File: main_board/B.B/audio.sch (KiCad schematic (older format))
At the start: 34 parts

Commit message: konzultace_s_Kubou_01
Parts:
- added C?: 1uf, Resistor_SMD:R_0402_1005Metric, symbol Device:C
- added C? (x2): 0.1uf, Resistor_SMD:R_0402_1005Metric, symbol Device:C
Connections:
- net 5V: now also C?.1, C?.1
- net at U?.4 (PB): now also C?.1
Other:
- moved on the sheet: C?, J?, LS?, MK?, R?, e

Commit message: preparation_to_drawing_PCB
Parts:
- J?: footprint (none) -> BB:JC-128
- LS? (x2), MK? (x2): footprint (none) -> Connector_PinHeader_2.54mm:PinHeader_1x02_P2.54mm_Vertical
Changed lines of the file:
@@
 F 0 "LS?" H 4070 5346 50  0000 L CNN
 F 1 "Speaker" H 4070 5255 50  0000 L CNN
-F 2 "" H 3900 5150 50  0001 C CNN
+F 2 "Connector_PinHeader_2.54mm:PinHeader_1x02_P2.54mm_Vertical" H 3900 5150 50  0001 C CNN
 F 3 "~" H 3890 5300 50  0001 C CNN
 	1    3900 5350
@@
 F 0 "LS?" H 4070 5046 50  0000 L CNN
 F 1 "Speaker" H 4070 4955 50  0000 L CNN
-F 2 "" H 3900 4850 50  0001 C CNN
+F 2 "Connector_PinHeader_2.54mm:PinHeader_1x02_P2.54mm_Vertical" H 3900 4850 50  0001 C CNN
 F 3 "~" H 3890 5000 50  0001 C CNN
 	1    3900 5050
@@
 F 0 "MK?" H 8670 5004 50  0000 R CNN
 F 1 "Microphone" H 8670 5095 50  0000 R CNN
-F 2 "" V 8800 5150 50  0001 C CNN
+F 2 "Connector_PinHeader_2.54mm:PinHeader_1x02_P2.54mm_Vertical" V 8800 5150 50  0001 C CNN
 F 3 "~" V 8800 5150 50  0001 C CNN
 	1    8800 5050
@@
 F 0 "MK?" H 10070 5004 50  0000 R CNN
 F 1 "Microphone" H 10070 5095 50  0000 R CNN
-F 2 "" V 10200 5150 50  0001 C CNN
+F 2 "Connector_PinHeader_2.54mm:PinHeader_1x02_P2.54mm_Vertical" V 10200 5150 50  0001 C CNN
 F 3 "~" V 10200 5150 50  0001 C CNN
 	1    10200 5050
@@
 F 0 "J?" H 9520 2833 50  0000 R CNN
 F 1 "AudioJack4" H 9520 2924 50  0000 R CNN
-F 2 "" H 9850 2950 50  0001 C CNN
+F 2 "BB:JC-128" H 9850 2950 50  0001 C CNN
 F 3 "~" H 9850 2950 50  0001 C CNN
 	1    9850 2950

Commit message: complete_preparation_to_drawing_PCB
footprint for all component and LCSC code for everything for mounting in JLCPCB
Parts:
- e1: renamed from e; footprint Package_DFN_QFN:QFN-20-1EP_4x4mm_P0.5mm_EP2.7x2.7mm -> Package_DFN_QFN:QFN-20-1EP_4x4mm_P0.5mm_EP2.5x2.5mm
- gave numbers to parts that had none: 36

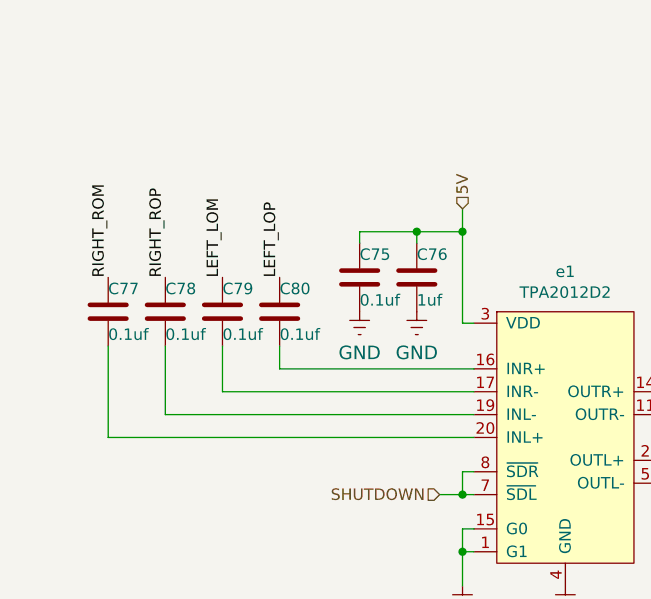
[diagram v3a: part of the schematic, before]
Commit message: optimalizace_kondenzatoru
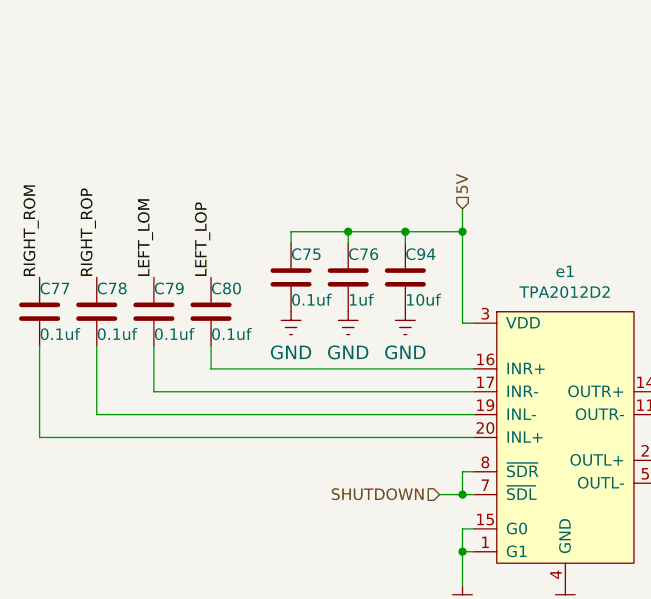
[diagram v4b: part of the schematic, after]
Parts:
- added C94: 10uf, Resistor_SMD:R_0603_1608Metric, symbol Device:C
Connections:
- net 5V: now also C94.1
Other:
- moved on the sheet: C75, C76, C77, C78, C79, C80
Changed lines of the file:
@@
 Text Label 7550 1900 0    50   ~ 0
 LEFT_LOP
-Text Label 1300 4550 1    50   ~ 0
+Text Label 1000 4550 1    50   ~ 0
 RIGHT_ROM
-Text Label 1550 4550 1    50   ~ 0
+Text Label 1250 4550 1    50   ~ 0
 RIGHT_ROP
-Text Label 1800 4550 1    50   ~ 0
+Text Label 1500 4550 1    50   ~ 0
 LEFT_LOM
-Text Label 2050 4550 1    50   ~ 0
+Text Label 1750 4550 1    50   ~ 0
 LEFT_LOP
-Wire Wire Line
-	2850 4250 2850 4350
 Wire Wire Line
 	2850 4750 2900 4750
@@
 L Device:C C80
 U 1 1 5F8B4EB8
-P 2050 4700
-F 0 "C80" H 2050 4800 50  0000 L CNN
-F 1 "0.1uf" H 2050 4600 50  0000 L CNN
-F 2 "Resistor_SMD:R_0402_1005Metric" H 2088 4550 50  0001 C CNN
-F 3 "~" H 2050 4700 50  0001 C CNN
-F 4 "C1525" H 2050 4700 50  0001 C CNN "LCSC"
-	1    2050 4700
-	1    0    0    -1
-$EndComp
-Wire Wire Line
-	2900 4950 2050 4950
-Wire Wire Line
-	2050 4950 2050 4850
+P 1750 4700
+F 0 "C80" H 1750 4800 50  0000 L CNN
+F 1 "0.1uf" H 1750 4600 50  0000 L CNN
+F 2 "Resistor_SMD:R_0402_1005Metric" H 1788 4550 50  0001 C CNN
+F 3 "~" H 1750 4700 50  0001 C CNN
+F 4 "C1525" H 1750 4700 50  0001 C CNN "LCSC"
+	1    1750 4700
+	1    0    0    -1
+$EndComp
+Wire Wire Line
+	2900 4950 1750 4950
+Wire Wire Line
+	1750 4950 1750 4850
 $Comp
 L Device:C C79
 U 1 1 5F8B62DA
-P 1800 4700
-F 0 "C79" H 1800 4800 50  0000 L CNN
-F 1 "0.1uf" H 1800 4600 50  0000 L CNN
-F 2 "Resistor_SMD:R_0402_1005Metric" H 1838 4550 50  0001 C CNN
-F 3 "~" H 1800 4700 50  0001 C CNN
-F 4 "C1525" H 1800 4700 50  0001 C CNN "LCSC"
-	1    1800 4700
+P 1500 4700
+F 0 "C79" H 1500 4800 50  0000 L CNN
+F 1 "0.1uf" H 1500 4600 50  0000 L CNN
+F 2 "Resistor_SMD:R_0402_1005Metric" H 1538 4550 50  0001 C CNN
+F 3 "~" H 1500 4700 50  0001 C CNN
+F 4 "C1525" H 1500 4700 50  0001 C CNN "LCSC"
+	1    1500 4700
 	1    0    0    -1
 $EndComp
@@
 L Device:C C78
 U 1 1 5F8B6561
-P 1550 4700
-F 0 "C78" H 1550 4800 50  0000 L CNN
-F 1 "0.1uf" H 1550 4600 50  0000 L CNN
-F 2 "Resistor_SMD:R_0402_1005Metric" H 1588 4550 50  0001 C CNN
-F 3 "~" H 1550 4700 50  0001 C CNN
-F 4 "C1525" H 1550 4700 50  0001 C CNN "LCSC"
-	1    1550 4700
+P 1250 4700
+F 0 "C78" H 1250 4800 50  0000 L CNN
+F 1 "0.1uf" H 1250 4600 50  0000 L CNN
+F 2 "Resistor_SMD:R_0402_1005Metric" H 1288 4550 50  0001 C CNN
+F 3 "~" H 1250 4700 50  0001 C CNN
+F 4 "C1525" H 1250 4700 50  0001 C CNN "LCSC"
+	1    1250 4700
 	1    0    0    -1
 $EndComp
@@
 L Device:C C77
 U 1 1 5F8B671A
-P 1300 4700
-F 0 "C77" H 1300 4800 50  0000 L CNN
-F 1 "0.1uf" H 1300 4600 50  0000 L CNN
-F 2 "Resistor_SMD:R_0402_1005Metric" H 1338 4550 50  0001 C CNN
-F 3 "~" H 1300 4700 50  0001 C CNN
-F 4 "C1525" H 1300 4700 50  0001 C CNN "LCSC"
-	1    1300 4700
-	1    0    0    -1
-$EndComp
-Wire Wire Line
-	2900 5050 1800 5050
-Wire Wire Line
-	1800 5050 1800 4850
-Wire Wire Line
-	1550 4850 1550 5150
-Wire Wire Line
-	1550 5150 2900 5150
-Wire Wire Line
-	2900 5250 1300 5250
-Wire Wire Line
-	1300 5250 1300 4850
+P 1000 4700
+F 0 "C77" H 1000 4800 50  0000 L CNN
+F 1 "0.1uf" H 1000 4600 50  0000 L CNN
+F 2 "Resistor_SMD:R_0402_1005Metric" H 1038 4550 50  0001 C CNN
+F 3 "~" H 1000 4700 50  0001 C CNN
+F 4 "C1525" H 1000 4700 50  0001 C CNN "LCSC"
+	1    1000 4700
+	1    0    0    -1
+$EndComp
+Wire Wire Line
+	2900 5050 1500 5050
+Wire Wire Line
+	1500 5050 1500 4850
+Wire Wire Line
+	1250 4850 1250 5150
+Wire Wire Line
+	2900 5250 1000 5250
+Wire Wire Line
+	1000 5250 1000 4850
 $Comp
 L B.B-eagle-import:GND #GND084
@@
 L Device:C C76
 U 1 1 5FA27E09
-P 2650 4550
-F 0 "C76" H 2650 4650 50  0000 L CNN
-F 1 "1uf" H 2650 4450 50  0000 L CNN
-F 2 "Resistor_SMD:R_0402_1005Metric" H 2688 4400 50  0001 C CNN
-F 3 "~" H 2650 4550 50  0001 C CNN
-F 4 "C52923" H 2650 4550 50  0001 C CNN "LCSC"
-	1    2650 4550
+P 2350 4550
+F 0 "C76" H 2350 4650 50  0000 L CNN
+F 1 "1uf" H 2350 4450 50  0000 L CNN
+F 2 "Resistor_SMD:R_0402_1005Metric" H 2388 4400 50  0001 C CNN
+F 3 "~" H 2350 4550 50  0001 C CNN
+F 4 "C52923" H 2350 4550 50  0001 C CNN "LCSC"
+	1    2350 4550
 	1    0    0    -1
 $EndComp
@@
 L B.B-eagle-import:GND #GND080
 U 1 1 5FA27E0F
-P 2650 4800
-F 0 "#GND080" H 2650 4800 50  0001 C CNN
-F 1 "GND" H 2650 4720 59  0000 C CNN
-F 2 "" H 2650 4800 50  0001 C CNN
-F 3 "" H 2650 4800 50  0001 C CNN
-	1    2650 4800
-	1    0    0    -1
-$EndComp
-Wire Wire Line
-	2650 4400 2650 4350
+P 2350 4800
+F 0 "#GND080" H 2350 4800 50  0001 C CNN
+F 1 "GND" H 2350 4720 59  0000 C CNN
+F 2 "" H 2350 4800 50  0001 C CNN
+F 3 "" H 2350 4800 50  0001 C CNN
+	1    2350 4800
+	1    0    0    -1
+$EndComp
+Wire Wire Line
+	2350 4400 2350 4350
 $Comp
 L Device:C C75
 U 1 1 5FA29F81
-P 2400 4550
-F 0 "C75" H 2400 4650 50  0000 L CNN
-F 1 "0.1uf" H 2400 4450 50  0000 L CNN
-F 2 "Resistor_SMD:R_0402_1005Metric" H 2438 4400 50  0001 C CNN
-F 3 "~" H 2400 4550 50  0001 C CNN
-F 4 "C1525" H 2400 4550 50  0001 C CNN "LCSC"
-	1    2400 4550
+P 2100 4550
+F 0 "C75" H 2100 4650 50  0000 L CNN
+F 1 "0.1uf" H 2100 4450 50  0000 L CNN
+F 2 "Resistor_SMD:R_0402_1005Metric" H 2138 4400 50  0001 C CNN
+F 3 "~" H 2100 4550 50  0001 C CNN
+F 4 "C1525" H 2100 4550 50  0001 C CNN "LCSC"
+	1    2100 4550
 	1    0    0    -1
 $EndComp
@@
 L B.B-eagle-import:GND #GND079
 U 1 1 5FA29F87
-P 2400 4800
-F 0 "#GND079" H 2400 4800 50  0001 C CNN
-F 1 "GND" H 2400 4720 59  0000 C CNN
-F 2 "" H 2400 4800 50  0001 C CNN
-F 3 "" H 2400 4800 50  0001 C CNN
-	1    2400 4800
-	1    0    0    -1
-$EndComp
-Wire Wire Line
-	2400 4400 2400 4350
-Wire Wire Line
-	2400 4350 2650 4350
-Connection ~ 2850 4350
-Wire Wire Line
-	2850 4350 2850 4750
-Connection ~ 2650 4350
-Wire Wire Line
-	2650 4350 2850 4350
+P 2100 4800
+F 0 "#GND079" H 2100 4800 50  0001 C CNN
+F 1 "GND" H 2100 4720 59  0000 C CNN
+F 2 "" H 2100 4800 50  0001 C CNN
+F 3 "" H 2100 4800 50  0001 C CNN
+	1    2100 4800
+	1    0    0    -1
+$EndComp
+Wire Wire Line
+	2100 4400 2100 4350
+Wire Wire Line
+	2100 4350 2350 4350
+Connection ~ 2350 4350
 Connection ~ 5050 2000
 Wire Wire Line
@@
 Wire Wire Line
 	4750 2150 4700 2150
+Wire Wire Line
+	2850 4250 2850 4350
+$Comp
+L B.B-eagle-import:GND #GND098
+U 1 1 5FB00FAA
+P 2600 4800
+F 0 "#GND098" H 2600 4800 50  0001 C CNN
+F 1 "GND" H 2600 4720 59  0000 C CNN
+F 2 "" H 2600 4800 50  0001 C CNN
+F 3 "" H 2600 4800 50  0001 C CNN
+	1    2600 4800
+	1    0    0    -1
+$EndComp
+$Comp
+L Device:C C94
+U 1 1 5FB00FB1
+P 2600 4550
+F 0 "C94" H 2600 4650 50  0000 L CNN
+F 1 "10uf" H 2600 4450 50  0000 L CNN
+F 2 "Resistor_SMD:R_0603_1608Metric" H 2638 4400 50  0001 C CNN
+F 3 "~" H 2600 4550 50  0001 C CNN
+F 4 "C19702" H 2600 4550 50  0001 C CNN "LCSC"
+	1    2600 4550
+	1    0    0    -1
+$EndComp
+Wire Wire Line
+	2600 4400 2600 4350
+Wire Wire Line
+	1250 5150 2900 5150
+Wire Wire Line
+	2350 4350 2600 4350
+Connection ~ 2850 4350
+Wire Wire Line
+	2850 4350 2850 4750
+Connection ~ 2600 4350
+Wire Wire Line
+	2600 4350 2850 4350
 $EndSCHEMATC

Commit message: start vith pcb
firsxxt proposal component layout of main board
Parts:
- removed J4: AudioJack4, BB:JC-128, symbol Connector:AudioJack4
- added J4: AudioJack4, BB:JC-128, symbol B.B-rescue:AudioJack4
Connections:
- net HPLOUT: now also J4.5
- net HPROUT: now also J4.3, J4.4
- net MIC2L: now also J4.2
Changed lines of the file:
@@
 EESchema Schematic File Version 4
-LIBS:B.B-cache
-EELAYER 29 0
+EELAYER 30 0
 EELAYER END
 $Descr A4 11693 8268
@@
 	9950 4850 10200 4850
 Connection ~ 10200 4850
-$Comp
-L Connector:AudioJack4 J4
-U 1 1 5F9F0C6D
-P 9850 2950
-F 0 "J4" H 9520 2833 50  0000 R CNN
-F 1 "AudioJack4" H 9520 2924 50  0000 R CNN
-F 2 "BB:JC-128" H 9850 2950 50  0001 C CNN
-F 3 "~" H 9850 2950 50  0001 C CNN
-	1    9850 2950
-	-1   0    0    1
-$EndComp
 Connection ~ 3950 1600
 $Comp
@@
 Wire Wire Line
 	2600 4350 2850 4350
+$Comp
+L B.B-rescue:AudioJack4 J4
+U 1 1 5FAE8ECF
+P 9850 2950
+F 0 "J4" H 9520 2833 50  0000 R CNN
+F 1 "AudioJack4" H 9520 2924 50  0000 R CNN
+F 2 "BB:JC-128" H 9850 2950 50  0001 C CNN
+F 3 "~" H 9850 2950 50  0001 C CNN
+	1    9850 2950
+	-1   0    0    1
+$EndComp
 $EndSCHEMATC
